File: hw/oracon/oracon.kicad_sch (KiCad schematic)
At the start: 101 parts, among them J1 DE9_Pins_MountingHoles, J2 SIM_Card, J3 USB_A, J5 USB_C_Receptacle_USB2.0_16P, Q1 SS8050, Q2 SS8050, Q3 SS8050, Q5 SS8050, SW1 SW_Push, U1 TP5100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

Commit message: Work on PCB, renamed KiCad project
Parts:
- added J4: Conn_Coaxial, symbol Connector:Conn_Coaxial
- J3: footprint Connector_USB:USB_A_Molex_67643_Horizontal -> kolskypavel:HYC214-USBA04-113
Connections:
- net GND: now also J4.2 (Ext); no longer J3.5 (Shield)
- net at J1.2: now also U6.13 (R1IN); no longer U6.14 (T1OUT)
- net at J1.3: now also U6.14 (T1OUT); no longer U6.13 (R1IN)
- net at R32.1: now also J4.1 (In)
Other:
- title: nbiot_esp32s3_hat -> Oracon
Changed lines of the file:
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@@
 	(paper "A3")
 	(title_block
-		(title "nbiot_esp32s3_hat")
-		(date "2025-04-25")
+		(title "Oracon")
+		(date "2025-10-04")
 		(company "kolskypavel")
 	)
@@
 	)
 	(junction
-		(at 377.19 173.99)
-		(diameter 0)
-		(color 0 0 0 0)
-	)
-	(junction
 		(at 397.51 63.5)
 		(diameter 0)
@@
 	(wire
 		(pts
-			(xy 374.65 173.99) (xy 377.19 173.99)
-		)
-		(stroke
-			(width 0)
-			(type default)
-		)
-	)
-	(wire
-		(pts
 			(xy 62.23 29.21) (xy 62.23 31.75)
 		)
@@
 	(wire
 		(pts
-			(xy 377.19 172.72) (xy 377.19 173.99)
+			(xy 377.19 172.72) (xy 377.19 175.26)
 		)
 		(stroke
@@
 	(wire
 		(pts
-			(xy 374.65 172.72) (xy 374.65 173.99)
-		)
-		(stroke
-			(width 0)
-			(type default)
-		)
-	)
-	(wire
-		(pts
 			(xy 52.07 237.49) (xy 72.39 237.49)
 		)
@@
 	(wire
 		(pts
-			(xy 358.14 227.33) (xy 364.49 227.33)
+			(xy 34.29 87.63) (xy 34.29 86.36)
 		)
 		(stroke
@@
 	(wire
 		(pts
-			(xy 34.29 87.63) (xy 34.29 86.36)
+			(xy 334.01 222.25) (xy 364.49 222.25)
 		)
 		(stroke
@@
 	(wire
 		(pts
-			(xy 355.6 227.33) (xy 355.6 222.25)
-		)
-		(stroke
-			(width 0)
-			(type default)
-		)
-	)
-	(wire
-		(pts
 			(xy 245.11 271.78) (xy 257.81 271.78)
 		)
@@
 	(wire
 		(pts
-			(xy 355.6 222.25) (xy 364.49 222.25)
+			(xy 363.22 87.63) (xy 370.84 87.63)
 		)
 		(stroke
@@
 	(wire
 		(pts
-			(xy 363.22 87.63) (xy 370.84 87.63)
+			(xy 184.15 52.07) (xy 184.15 62.23)
 		)
 		(stroke
@@
 	(wire
 		(pts
-			(xy 184.15 52.07) (xy 184.15 62.23)
+			(xy 397.51 24.13) (xy 397.51 39.37)
 		)
 		(stroke
@@
 	(wire
 		(pts
-			(xy 397.51 24.13) (xy 397.51 39.37)
+			(xy 378.46 63.5) (xy 386.08 63.5)
 		)
 		(stroke
@@
 	(wire
 		(pts
-			(xy 378.46 63.5) (xy 386.08 63.5)
+			(xy 30.48 224.79) (xy 100.33 224.79)
 		)
 		(stroke
@@
 	(wire
 		(pts
-			(xy 30.48 224.79) (xy 100.33 224.79)
+			(xy 326.39 217.17) (xy 334.01 217.17)
 		)
 		(stroke
@@
 	(wire
 		(pts
+			(xy 137.16 177.8) (xy 146.05 177.8)
+		)
+		(stroke
+			(width 0)
+			(type default)
+		)
+	)
+	(wire
+		(pts
 			(xy 147.32 53.34) (xy 151.13 53.34)
 		)
@@
 	(wire
 		(pts
-			(xy 377.19 173.99) (xy 377.19 175.26)
-		)
-		(stroke
-			(width 0)
-			(type default)
-		)
-	)
-	(wire
-		(pts
 			(xy 205.74 265.43) (xy 205.74 261.62)
 		)
@@
 	(wire
 		(pts
-			(xy 46.99 24.13) (xy 45.72 24.13)
+			(xy 151.13 182.88) (xy 151.13 190.5)
 		)
 		(stroke
@@
 	(wire
 		(pts
-			(xy 22.86 62.23) (xy 22.86 63.5)
+			(xy 46.99 24.13) (xy 45.72 24.13)
 		)
 		(stroke
@@
 	(wire
 		(pts
-			(xy 34.29 95.25) (xy 34.29 96.52)
+			(xy 22.86 62.23) (xy 22.86 63.5)
 		)
 		(stroke
@@
 	(wire
 		(pts
-			(xy 326.39 217.17) (xy 358.14 217.17)
+			(xy 34.29 95.25) (xy 34.29 96.52)
 		)
 		(stroke
@@
 	(wire
 		(pts
-			(xy 358.14 217.17) (xy 358.14 227.33)
-		)
-		(stroke
-			(width 0)
-			(type default)
-		)
-	)
-	(wire
-		(pts
 			(xy 182.88 264.16) (xy 184.15 264.16)
 		)
@@
 	(wire
 		(pts
-			(xy 326.39 227.33) (xy 355.6 227.33)
+			(xy 326.39 227.33) (xy 364.49 227.33)
 		)
 		(stroke
@@
 	(wire
 		(pts
+			(xy 334.01 222.25) (xy 334.01 217.17)
+		)
+		(stroke
+			(width 0)
+			(type default)
+		)
+	)
+	(wire
+		(pts
 			(xy 384.81 58.42) (xy 386.08 58.42)
 		)
@@
 		(dnp no)
 		(property "Reference" "C22"
-			(at 342.9 215.392 0)
+			(at 341.884 216.662 90)
 			(effects
 				(font
@@
 		)
 		(property "Value" "100n"
-			(at 340.36 215.392 0)
+			(at 340.868 218.948 90)
 			(effects
 				(font
@@
 			)
 		)
-		(property "Footprint" "Connector_USB:USB_A_Molex_67643_Horizontal"
+		(property "Footprint" "kolskypavel:HYC214-USBA04-113"
 			(at 381 163.83 0)
 			(effects
@@
 		(pin "3"
 		)
-		(pin "5"
-		)
 		(pin "1"
 		)
@@
 					(unit 1)
 				)
+			)
+		)
+	)
+	(symbol
+		(lib_id "Connector:Conn_Coaxial")
+		(at 151.13 177.8 0)
+		(unit 1)
+		(exclude_from_sim no)
+		(in_bom yes)
+		(on_board yes)
+		(dnp no)
+		(fields_autoplaced yes)
+		(property "Reference" "J4"
+			(at 154.94 176.8231 0)
+			(effects
+				(font
+					(size 1.27 1.27)
+				)
+				(justify left)
+			)
+		)
+		(property "Value" "Conn_Coaxial"
+			(at 154.94 179.3631 0)
+			(effects
+				(font
+					(size 1.27 1.27)
+				)
+				(justify left)
+			)
+		)
+		(property "Footprint" ""
+			(at 151.13 177.8 0)
+			(effects
+				(font
+					(size 1.27 1.27)
+				)
+				(hide yes)
+			)
+		)
+		(property "Datasheet" "~"
+			(at 151.13 177.8 0)
+			(effects
+				(font
+					(size 1.27 1.27)
+				)
+				(hide yes)
+			)
+		)
+		(property "Description" "coaxial connector (BNC, SMA, SMB, SMC, Cinch/RCA, LEMO, ...)"
+			(at 151.13 177.8 0)
+			(effects
+				(font
+					(size 1.27 1.27)
+				)
+				(hide yes)
+			)
+		)
+		(pin "1"
+		)
+		(pin "2"
+		)
+		(instances
+			(project ""
+				(path "/7501ec1f-5c34-40ce-b7e3-cacc6e1961d1"
+					(reference "J4")
+					(unit 1)
+				)

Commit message: PCB layout - init
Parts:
- removed J1: DE9_Pins_MountingHoles, Connector_Dsub:DSUB-9_Pins_Horizontal_P2.77x2.84mm_EdgePinOffset4.94mm_Housed_MountingHolesOffset4.94mm, symbol Connector:DE9_Pins_MountingHoles
- added TP5: Serial_TX, TestPoint:TestPoint_Pad_D1.5mm, symbol Connector:TestPoint
- added TP6: Serial_RX, TestPoint:TestPoint_Pad_D1.5mm, symbol Connector:TestPoint
- added TP7: Serial_GND, TestPoint:TestPoint_Pad_D1.5mm, symbol Connector:TestPoint
- J4: footprint (none) -> kolskypavel:IPEX-SMD_4P-L1.8-W1.7-LS2.0
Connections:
- net GND: now also J4.3 (Ext), J4.4 (Ext), TP7.1
- net at U6.13 (R1IN): now also TP6.1
- net at U6.14 (T1OUT): now also TP5.1

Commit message: PCB work, back to basics  :D
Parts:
- J5: footprint Connector_USB:USB_C_Receptacle_GCT_USB4105-xx-A_16P_TopMnt_Horizontal -> kolskypavel:HOAUC HYCW412-USBC16-065B
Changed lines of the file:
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@@
 			)
 		)
-		(property "Footprint" "Connector_USB:USB_C_Receptacle_GCT_USB4105-xx-A_16P_TopMnt_Horizontal"
+		(property "Footprint" "kolskypavel:HOAUC HYCW412-USBC16-065B"
 			(at 34.29 39.37 0)
 			(effects

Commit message: Further PCB work - almost ready
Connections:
- net CHG_STAT: now also U3.26 (IO26); no longer U3.29 (IO34)
- net LED1_G: now also U3.37 (IO41); no longer U3.36 (IO40)
- net LED1_R: now also U3.36 (IO40); no longer U3.37 (IO41)
- net LED2_G: now also U3.34 (IO38); no longer U3.33 (IO37)
- net LED2_R: now also U3.33 (IO37); no longer U3.34 (IO38)
- net LED3_B: now also U3.30 (IO48); no longer U3.6 (IO2)
- net LED3_G: now also U3.29 (IO34); no longer U3.7 (IO3)
- net LED3_R: now also U3.28 (IO33); no longer U3.8 (IO4)
- net RS232_RX: now also U3.6 (IO2); no longer U3.17 (IO13)
- net RS232_TX: now also U3.5 (IO1); no longer U3.16 (IO12)
- net SIM_CLK: now also U7.16 (SIM_CLK)
- net SIM_DATA: now also U7.15 (SIM_DATA)
- net SIM_RST: now also U7.17 (SIM_RST)
- net SIM_VDD: now also U7.18 (SIM_VDD)
- net STBY_STAT: now also U3.27 (IO47); no longer U3.28 (IO33)
- net USB_SI_N: now also U3.7 (IO3); no longer U3.23 (IO19)
- net USB_SI_P: now also U3.8 (IO4); no longer U3.24 (IO20)
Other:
- moved on the sheet: C12, C13, C14, R7

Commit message: PCB work, paths and zones
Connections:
- net VBAT is gone; now on net +3.3V: C36.1, C37.1, U7.34 (VBAT), U7.35 (VBAT)
- net GND: now also J2.8 (SH)
- net NBIOT_RX: now also U7.1 (UART1_TXD); no longer U7.22 (UART0_TXD)
- net NBIOT_TX: now also U7.2 (UART1_RXD); no longer U7.23 (UART0_RXD)
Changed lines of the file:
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@@
 	(wire
 		(pts
-			(xy 219.71 135.89) (xy 208.28 135.89)
-		)
-		(stroke
-			(width 0)
-			(type default)
-		)
-	)
-	(wire
-		(pts
 			(xy 175.26 31.75) (xy 144.78 31.75)
 		)
@@
 	(wire
 		(pts
+			(xy 217.17 135.89) (xy 208.28 135.89)
+		)
+		(stroke
+			(width 0)
+			(type default)
+		)
+	)
+	(wire
+		(pts
 			(xy 276.86 73.66) (xy 311.15 73.66)
 		)
@@
 		)
 	)
+	(global_label "NBIOT_RX"
+		(shape input)
+		(at 140.97 121.92 180)
+		(fields_autoplaced yes)
+		(effects
+			(font
+				(size 1.27 1.27)
+			)
+			(justify right)
+		)
+		(property "Intersheetrefs" "${INTERSHEET_REFS}"
+			(at 129.0343 121.92 0)
+			(effects
+				(font
+					(size 1.27 1.27)
+				)
+				(justify right)
+				(hide yes)
+			)
+		)
+	)
 	(global_label "LED3_B"
 		(shape input)
@@
 		)
 	)
-	(global_label "NBIOT_TX"
+	(global_label "LED1_B"
 		(shape input)
-		(at 191.77 121.92 0)
+		(at 78.74 137.16 0)
 		(fields_autoplaced yes)
 		(effects
@@
 		)
 		(property "Intersheetrefs" "${INTERSHEET_REFS}"
-			(at 203.4033 121.92 0)
+			(at 88.6194 137.16 0)
 			(effects
 				(font
@@
 		)
 	)
-	(global_label "LED1_B"
+	(global_label "USB_SI_N"
 		(shape input)
-		(at 78.74 137.16 0)
+		(at 48.26 109.22 180)
 		(fields_autoplaced yes)
 		(effects
@@
 				(size 1.27 1.27)
 			)
-			(justify left)
+			(justify right)
 		)
 		(property "Intersheetrefs" "${INTERSHEET_REFS}"
-			(at 88.6194 137.16 0)
+			(at 36.3848 109.22 0)
 			(effects
 				(font
 					(size 1.27 1.27)
 				)
-				(justify left)
+				(justify right)
 				(hide yes)
 			)
 		)
 	)
-	(global_label "USB_SI_N"
+	(global_label "NBIOT_TX"
 		(shape input)
-		(at 48.26 109.22 180)
+		(at 140.97 124.46 180)
 		(fields_autoplaced yes)
 		(effects
@@
 		)
 		(property "Intersheetrefs" "${INTERSHEET_REFS}"
-			(at 36.3848 109.22 0)
+			(at 129.3367 124.46 0)
 			(effects
 				(font
@@
 		)
 	)
-	(global_label "NBIOT_RX"
-		(shape input)
-		(at 191.77 119.38 0)
-		(fields_autoplaced yes)
-		(effects
-			(font
-				(size 1.27 1.27)
-			)
-			(justify left)
-		)
-		(property "Intersheetrefs" "${INTERSHEET_REFS}"
-			(at 203.7057 119.38 0)
-			(effects
-				(font
-					(size 1.27 1.27)
-				)
-				(justify left)
-				(hide yes)
-			)
-		)
-	)
 	(global_label "LED2_B"
 		(shape input)
@@
 	(symbol
 		(lib_id "power:GND")
+		(at 119.38 248.92 0)
+		(unit 1)
+		(exclude_from_sim no)
+		(in_bom yes)
+		(on_board yes)
+		(dnp no)
+		(fields_autoplaced yes)
+		(property "Reference" "#PWR030"
+			(at 119.38 255.27 0)
+			(effects
+				(font
+					(size 1.27 1.27)
+				)
+				(hide yes)
+			)
+		)
+		(property "Value" "GND"
+			(at 119.38 254 0)
+			(effects
+				(font
+					(size 1.27 1.27)
+				)
+			)
+		)
+		(property "Footprint" ""
+			(at 119.38 248.92 0)
+			(effects
+				(font
+					(size 1.27 1.27)
+				)
+				(hide yes)
+			)
+		)
+		(property "Datasheet" ""
+			(at 119.38 248.92 0)
+			(effects
+				(font
+					(size 1.27 1.27)
+				)
+				(hide yes)
+			)
+		)
+		(property "Description" "Power symbol creates a global label with name \"GND\" , ground"
+			(at 119.38 248.92 0)
+			(effects
+				(font
+					(size 1.27 1.27)
+				)
+				(hide yes)
+			)
+		)
+		(pin "1"
+		)
+		(instances
+			(project "oracon"
+				(path "/7501ec1f-5c34-40ce-b7e3-cacc6e1961d1"
+					(reference "#PWR030")
+					(unit 1)
+				)
+			)
+		)
+	)
+	(symbol
+		(lib_id "power:GND")
 		(at 190.5 154.94 0)
 		(unit 1)
@@
 	)
 	(symbol
+		(lib_id "power:+3.3V")
+		(at 217.17 135.89 0)
+		(unit 1)
+		(exclude_from_sim no)
+		(in_bom yes)
+		(on_board yes)
+		(dnp no)
+		(fields_autoplaced yes)
+		(property "Reference" "#PWR050"
+			(at 217.17 139.7 0)
+			(effects
+				(font
+					(size 1.27 1.27)
+				)
+				(hide yes)
+			)
+		)
+		(property "Value" "+3.3V"
+			(at 217.17 130.81 0)
+			(effects
+				(font
+					(size 1.27 1.27)
+				)
+			)
+		)
+		(property "Footprint" ""
+			(at 217.17 135.89 0)
+			(effects
+				(font
+					(size 1.27 1.27)
+				)
+				(hide yes)
+			)
+		)
+		(property "Datasheet" ""
+			(at 217.17 135.89 0)
+			(effects
+				(font
+					(size 1.27 1.27)
+				)
+				(hide yes)
+			)
+		)
+		(property "Description" "Power symbol creates a global label with name \"+3.3V\""
+			(at 217.17 135.89 0)
+			(effects
+				(font
+					(size 1.27 1.27)
+				)
+				(hide yes)
+			)
+		)
+		(pin "1"
+		)
+		(instances
+			(project "oracon"
+				(path "/7501ec1f-5c34-40ce-b7e3-cacc6e1961d1"
+					(reference "#PWR050")
+					(unit 1)
+				)
+			)
+		)
+	)
+	(symbol
 		(lib_id "Device:C")
 		(at 124.46 184.15 0)
@@
 	)
 	(symbol
-		(lib_id "power:+3.3V")
-		(at 219.71 135.89 0)
-		(unit 1)
-		(exclude_from_sim no)
-		(in_bom yes)
-		(on_board yes)
-		(dnp no)
-		(property "Reference" "#PWR051"
-			(at 219.71 139.7 0)
-			(effects
-				(font
-					(size 1.27 1.27)
-				)
-				(hide yes)
-			)
-		)
-		(property "Value" "VBAT"
-			(at 219.456 131.572 0)
-			(effects
-				(font
-					(size 1.27 1.27)
-				)
-			)
-		)
-		(property "Footprint" ""
-			(at 219.71 135.89 0)
-			(effects
-				(font
-					(size 1.27 1.27)
-				)
-				(hide yes)
-			)
-		)
-		(property "Datasheet" ""
-			(at 219.71 135.89 0)
-			(effects
-				(font
-					(size 1.27 1.27)
-				)
-				(hide yes)
-			)
-		)
-		(property "Description" "Power symbol creates a global label with name \"+3.3V\""
-			(at 219.71 135.89 0)
-			(effects
-				(font
-					(size 1.27 1.27)
-				)
-				(hide yes)
-			)
-		)
-		(pin "1"
-		)
-		(instances
-			(project "nbiot_esp32s3_hat"
-				(path "/7501ec1f-5c34-40ce-b7e3-cacc6e1961d1"
-					(reference "#PWR051")
-					(unit 1)
-				)
-			)
-		)
-	)
-	(symbol
 		(lib_id "Transistor_BJT:SS8050")
 		(at 327.66 25.4 0)
@@
 		(pin "2"
 		)
+		(pin "8"
+		)
+		(pin "9"
+		)
 		(instances

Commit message: Some PCB restruct
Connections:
- net GND: now also J2.SH; no longer J2.8 (SH)
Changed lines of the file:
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@@
 		(pin "2"
 		)
-		(pin "8"
+		(pin "CD"
 		)
-		(pin "9"
+		(pin "SH"
 		)
 		(instances

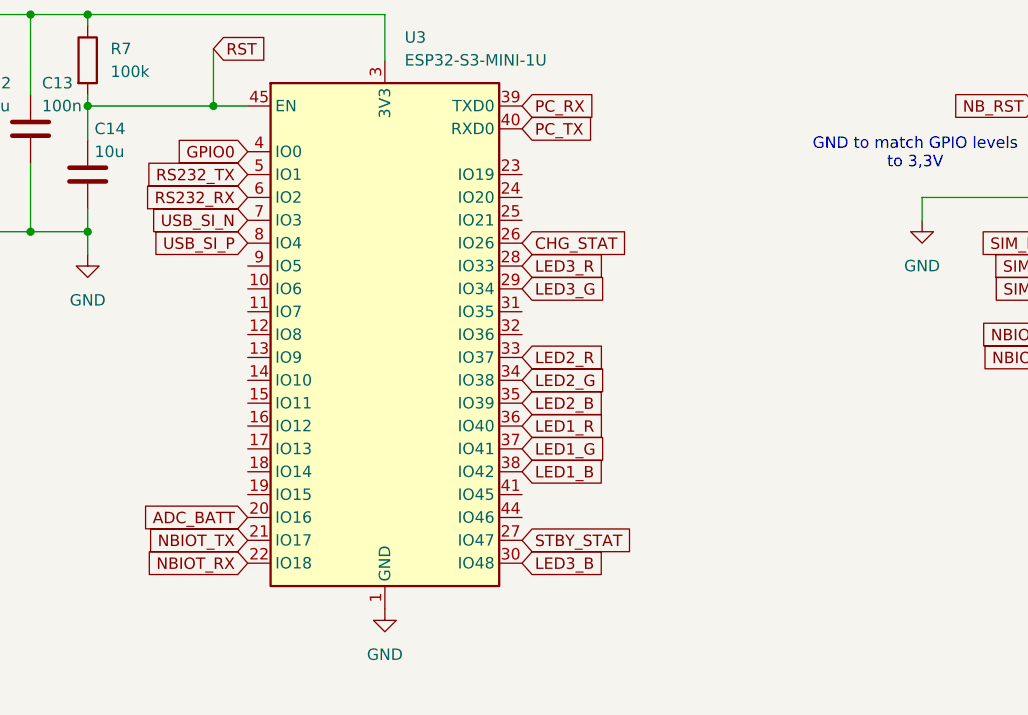
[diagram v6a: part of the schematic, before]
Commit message: Rerouted some ESP pins
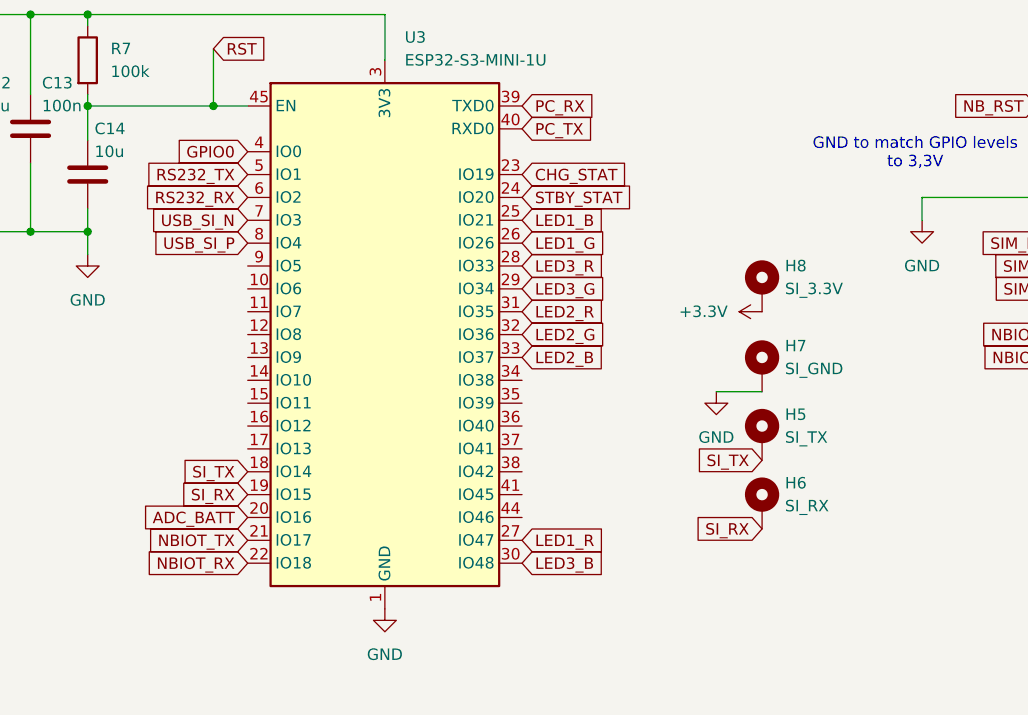
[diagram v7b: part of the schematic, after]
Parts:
- added H5: SI_TX, TestPoint:TestPoint_Pad_D1.5mm, symbol Mechanical:MountingHole_Pad
- added H6: SI_RX, TestPoint:TestPoint_Pad_D1.5mm, symbol Mechanical:MountingHole_Pad
- added H7: SI_GND, TestPoint:TestPoint_Pad_D1.5mm, symbol Mechanical:MountingHole_Pad
- added H8: SI_3.3V, TestPoint:TestPoint_Pad_D1.5mm, symbol Mechanical:MountingHole_Pad
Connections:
- net +3.3V: now also H8.1
- net CHG_STAT: now also U3.23 (IO19); no longer U3.26 (IO26)
- net GND: now also H7.1
- net LED1_B: now also U3.25 (IO21); no longer U3.38 (IO42)
- net LED1_G: now also U3.26 (IO26); no longer U3.37 (IO41)
- net LED1_R: now also U3.27 (IO47); no longer U3.36 (IO40)
- net LED2_B: now also U3.33 (IO37); no longer U3.35 (IO39)
- net LED2_G: now also U3.32 (IO36); no longer U3.34 (IO38)
- net LED2_R: now also U3.31 (IO35); no longer U3.33 (IO37)
- net STBY_STAT: now also U3.24 (IO20); no longer U3.27 (IO47)
- net SI_TX: now reaches U3.18 (IO14)
- net SI_TX: now also H5.1
- net SI_RX: now reaches U3.19 (IO15)
- net SI_RX: now also H6.1

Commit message: Further routing
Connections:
- net ADC_BATT: now also U3.18 (IO14); no longer U3.20 (IO16)
- net CHG_STAT: now also U3.21 (IO17); no longer U3.23 (IO19)
- net LED1_B: now also U3.11 (IO7); no longer U3.25 (IO21)
- net LED1_G: now also U3.12 (IO8); no longer U3.26 (IO26)
- net LED1_R: now also U3.13 (IO9); no longer U3.27 (IO47)
- net LED2_B: now also U3.38 (IO42); no longer U3.33 (IO37)
- net LED2_G: now also U3.37 (IO41); no longer U3.32 (IO36)
- net LED2_R: now also U3.36 (IO40); no longer U3.31 (IO35)
- net LED3_B: now also U3.35 (IO39); no longer U3.30 (IO48)
- net LED3_G: now also U3.34 (IO38); no longer U3.29 (IO34)
- net LED3_R: now also U3.33 (IO37); no longer U3.28 (IO33)
- net NBIOT_RX: now also U3.20 (IO16); no longer U3.22 (IO18)
- net NBIOT_TX: now also U3.19 (IO15); no longer U3.21 (IO17)
- net SI_RX: now also U3.17 (IO13); no longer U3.19 (IO15)
- net SI_TX: now also U3.16 (IO12); no longer U3.18 (IO14)
- net STBY_STAT: now also U3.22 (IO18); no longer U3.24 (IO20)
